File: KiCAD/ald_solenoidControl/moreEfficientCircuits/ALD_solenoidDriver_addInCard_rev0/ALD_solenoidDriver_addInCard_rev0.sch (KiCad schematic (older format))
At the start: 9 parts, among them U1 ASSR-1611

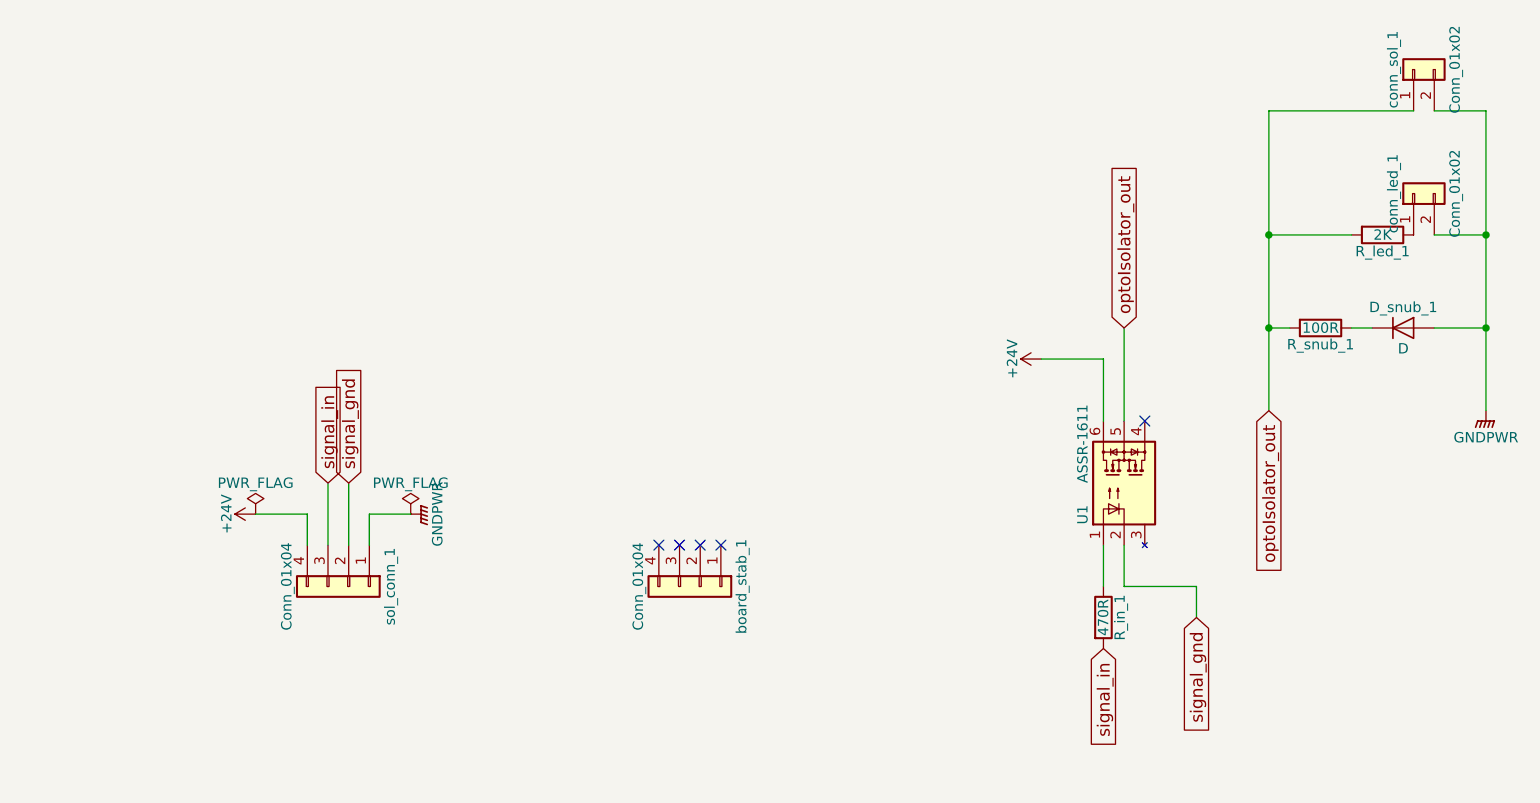
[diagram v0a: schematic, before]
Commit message: add mounting holes to add in card, make zones, move current limiting resistor
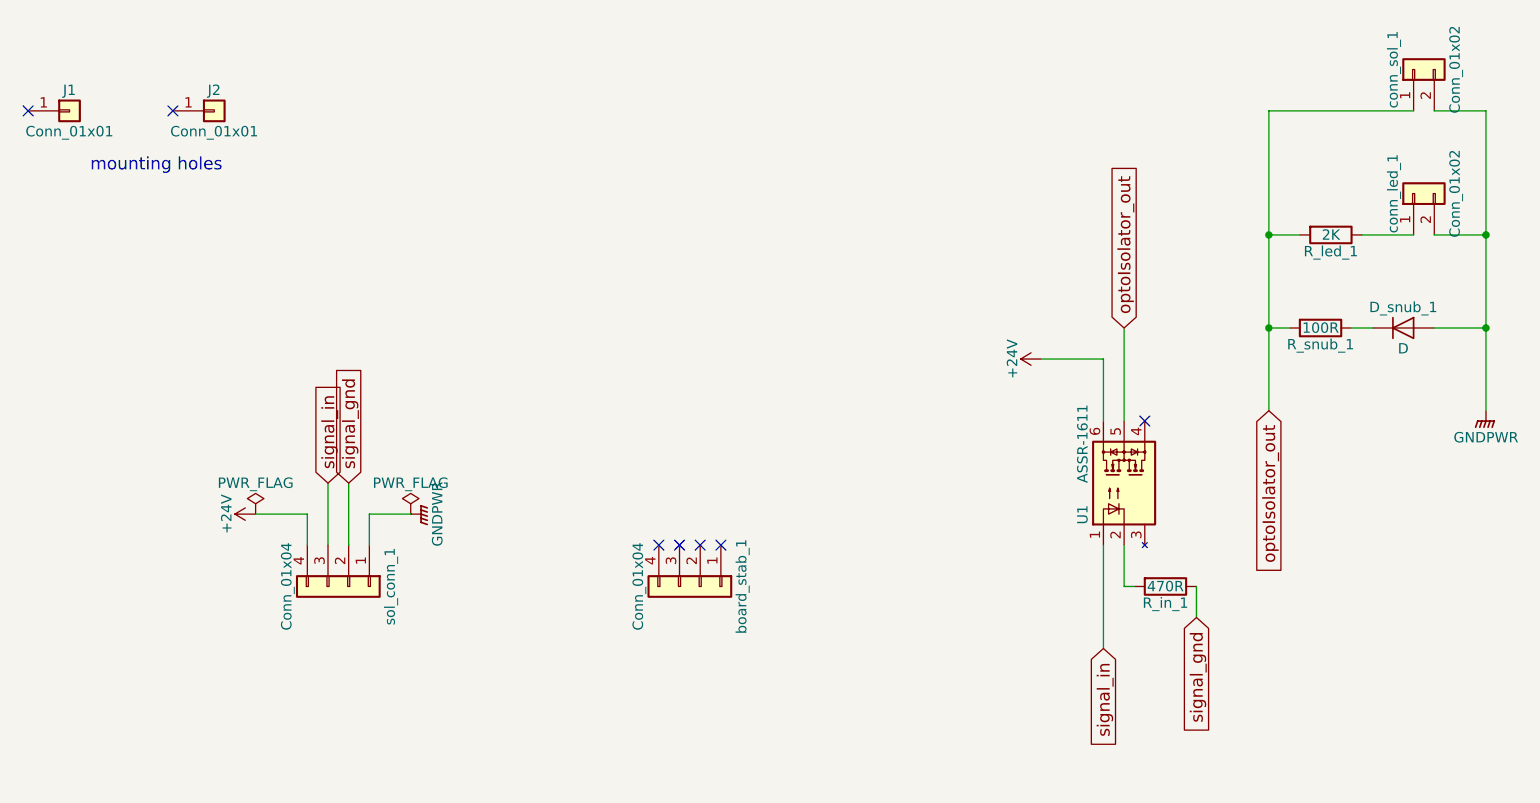
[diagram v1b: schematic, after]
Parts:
- added J1, J2: Conn_01x01, Mounting_Holes:MountingHole_3mm_Pad, symbol Conn_01x01
- D_snub_1: farnellCode (none) -> 1695714
- R_in_1, R_led_1, R_snub_1: footprint Resistors_THT:R_Axial_DIN0204_L3.6mm_D1.6mm_P7.62mm_Horizontal -> Resistors_SMD:R_2010_HandSoldering
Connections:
- net signal_gnd: now also R_in_1.1; no longer U1.2
- net signal_in: now also U1.1; no longer R_in_1.2
- new net: R_in_1.2, U1.2
- no-connect marks 5 -> 7
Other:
- note added: "mounting holes"
- moved on the sheet: R_in_1, R_led_1
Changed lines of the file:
@@
 EESchema Schematic File Version 2
+LIBS:ac-dc
+LIBS:adc-dac
+LIBS:Altera
+LIBS:analog_devices
+LIBS:analog_switches
+LIBS:atmel
+LIBS:audio
+LIBS:Battery_Management
+LIBS:bbd
+LIBS:Bosch
+LIBS:brooktre
+LIBS:Connector
+LIBS:contrib
+LIBS:cypress
+LIBS:dc-dc
+LIBS:device
+LIBS:digital-audio
+LIBS:Diode
+LIBS:Display
+LIBS:driver_gate
+LIBS:dsp
+LIBS:DSP_Microchip_DSPIC33
+LIBS:elec-unifil
+LIBS:ESD_Protection
+LIBS:Espressif
+LIBS:FPGA_Actel
+LIBS:ftdi
+LIBS:gennum
+LIBS:Graphic
+LIBS:hc11
+LIBS:infineon
+LIBS:intel
+LIBS:interface
+LIBS:intersil
+LIBS:ir
+LIBS:Lattice
+LIBS:LED
+LIBS:LEM
+LIBS:linear
+LIBS:Logic_74xgxx
+LIBS:Logic_74xx
+LIBS:Logic_CMOS_4000
+LIBS:Logic_CMOS_IEEE
+LIBS:logic_programmable
+LIBS:Logic_TTL_IEEE
+LIBS:maxim
+LIBS:MCU_Microchip_PIC10
+LIBS:MCU_Microchip_PIC12
+LIBS:MCU_Microchip_PIC16
+LIBS:MCU_Microchip_PIC18
+LIBS:MCU_Microchip_PIC24
+LIBS:MCU_Microchip_PIC32
+LIBS:MCU_NXP_Kinetis
+LIBS:MCU_NXP_LPC
+LIBS:MCU_NXP_S08
+LIBS:MCU_Parallax
+LIBS:MCU_ST_STM8
+LIBS:MCU_ST_STM32
+LIBS:MCU_Texas_MSP430
+LIBS:Mechanical
+LIBS:memory
+LIBS:microchip
+LIBS:microcontrollers
+LIBS:modules
+LIBS:Motor
+LIBS:motor_drivers
+LIBS:motorola
+LIBS:nordicsemi
+LIBS:nxp
+LIBS:onsemi
+LIBS:opto
+LIBS:Oscillators
+LIBS:philips
 LIBS:power
-LIBS:device
-LIBS:switches
-LIBS:relays
-LIBS:motors
-LIBS:transistors
-LIBS:conn
-LIBS:linear
+LIBS:powerint
+LIBS:Power_Management
+LIBS:pspice
+LIBS:references
 LIBS:regul
-LIBS:74xx
-LIBS:cmos4000
-LIBS:adc-dac
-LIBS:memory
+LIBS:Relay
+LIBS:rfcom
+LIBS:RFSolutions
+LIBS:Sensor_Current
+LIBS:sensors
+LIBS:silabs
+LIBS:siliconi
+LIBS:supertex
+LIBS:Switch
+LIBS:texas
+LIBS:Transformer
+LIBS:Transistor
+LIBS:triac_thyristor
+LIBS:Valve
+LIBS:video
+LIBS:wiznet
+LIBS:Worldsemi
+LIBS:Xicor
 LIBS:xilinx
-LIBS:microcontrollers
-LIBS:dsp
-LIBS:microchip
-LIBS:analog_switches
-LIBS:motorola
-LIBS:texas
-LIBS:intel
-LIBS:audio
-LIBS:interface
-LIBS:digital-audio
-LIBS:philips
-LIBS:display
-LIBS:cypress
-LIBS:siliconi
-LIBS:opto
-LIBS:atmel
-LIBS:contrib
-LIBS:valves
-LIBS:myParts
+LIBS:zetex
+LIBS:Zilog
+LIBS:ALD_solenoidDriver_addInCard_rev0-cache
 EELAYER 25 0
 EELAYER END
@@
 	7600 1600 7600 3050
 Wire Wire Line
-	6800 3700 6800 3900
+	6800 3700 6800 4200
 Wire Wire Line
 	6900 3700 6900 3900
-Wire Wire Line
-	6900 3900 7250 3900
 Wire Wire Line
 	7250 3900 7250 4050
@@
 L R R_in_1
 U 1 1 5A787113
-P 6800 4050
-F 0 "R_in_1" V 6880 4050 50  0000 C CNN
-F 1 "470R" V 6800 4050 50  0000 C CNN
-F 2 "Resistors_THT:R_Axial_DIN0204_L3.6mm_D1.6mm_P7.62mm_Horizontal" V 6730 4050 50  0001 C CNN
-F 3 "" H 6800 4050 50  0001 C CNN
-	1    6800 4050
-	1    0    0    -1
+P 7100 3900
+F 0 "R_in_1" V 7180 3900 50  0000 C CNN
+F 1 "470R" V 7100 3900 50  0000 C CNN
+F 2 "Resistors_SMD:R_2010_HandSoldering" V 7030 3900 50  0001 C CNN
+F 3 "" H 7100 3900 50  0001 C CNN
+	1    7100 3900
+	0    1    1    0
 $EndComp
 Text GLabel 6800 4200 3    60   Input ~ 0
@@
 F 0 "R_snub_1" V 7930 2650 50  0000 C CNN
 F 1 "100R" V 7850 2650 50  0000 C CNN
-F 2 "Resistors_THT:R_Axial_DIN0204_L3.6mm_D1.6mm_P7.62mm_Horizontal" V 7780 2650 50  0001 C CNN
+F 2 "Resistors_SMD:R_2010_HandSoldering" V 7780 2650 50  0001 C CNN
 F 3 "" H 7850 2650 50  0001 C CNN
 	1    7850 2650
@@
 F 2 "Diodes_THT:D_A-405_P7.62mm_Horizontal" H 8250 2650 50  0001 C CNN
 F 3 "" H 8250 2650 50  0001 C CNN
+F 4 "1695714" H 8250 2650 60  0001 C CNN "farnellCode"
 	1    8250 2650
 	1    0    0    -1
 $EndComp
-Wire Wire Line
-	7600 2200 8000 2200
 $Comp
 L R R_led_1
 U 1 1 5A78737C
-P 8150 2200
-F 0 "R_led_1" V 8230 2200 50  0000 C CNN
-F 1 "2K" V 8150 2200 50  0000 C CNN
-F 2 "Resistors_THT:R_Axial_DIN0204_L3.6mm_D1.6mm_P7.62mm_Horizontal" V 8080 2200 50  0001 C CNN
-F 3 "" H 8150 2200 50  0001 C CNN
-	1    8150 2200
+P 7900 2200
+F 0 "R_led_1" V 7980 2200 50  0000 C CNN
+F 1 "2K" V 7900 2200 50  0000 C CNN
+F 2 "Resistors_SMD:R_2010_HandSoldering" V 7830 2200 50  0001 C CNN
+F 3 "" H 7900 2200 50  0001 C CNN
+	1    7900 2200
 	0    1    1    0
 $EndComp
@@
 Text GLabel 6900 2650 1    60   Input ~ 0
 optoIsolator_out
+Wire Wire Line
+	6900 3900 6950 3900
+Wire Wire Line
+	7600 2200 7750 2200
+Wire Wire Line
+	8050 2200 8300 2200
+$Comp
+L Conn_01x01 J1
+U 1 1 5A858811
+P 1800 1600
+F 0 "J1" H 1800 1700 50  0000 C CNN
+F 1 "Conn_01x01" H 1800 1500 50  0000 C CNN
+F 2 "Mounting_Holes:MountingHole_3mm_Pad" H 1800 1600 50  0001 C CNN
+F 3 "" H 1800 1600 50  0001 C CNN
+	1    1800 1600
+	1    0    0    -1
+$EndComp
+$Comp
+L Conn_01x01 J2
+U 1 1 5A8588D2
+P 2500 1600
+F 0 "J2" H 2500 1700 50  0000 C CNN
+F 1 "Conn_01x01" H 2500 1500 50  0000 C CNN
+F 2 "Mounting_Holes:MountingHole_3mm_Pad" H 2500 1600 50  0001 C CNN
+F 3 "" H 2500 1600 50  0001 C CNN
+	1    2500 1600
+	1    0    0    -1
+$EndComp
+Text Notes 1900 1900 0    60   ~ 0
+mounting holes
+NoConn ~ 1600 1600
+NoConn ~ 2300 1600
 $EndSCHEMATC
